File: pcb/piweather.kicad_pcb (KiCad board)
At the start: 4 copper layers, 65 x 64 mm, 22 parts, among them J1 Screw_Terminal_01x10, J10 Conn_01x03_Male, J11 Conn_01x03_Male, J12 Conn_01x02_Male, J2 Conn_01x08_Male, J3 Screw_Terminal_01x02, J4 Raspberry_Pi_2_3, J5 Conn_01x03_Male, J6 Conn_01x01_Male, J7 Conn_01x01_Male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

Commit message: started passive placement
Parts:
- added C10: GRM21BR60J476ME15K, Main:CAPC0805, F.Cu at (96.1, 78.3)
- added C11: CC0603KRX7R9BB104, Main:CAPC0603, F.Cu at (158.1, 82.4)
- added C12: GRM21BR60J476ME15K, Main:CAPC0805, F.Cu at (111.1, 56.0)
- added C13: CC0603KRX7R9BB104, Main:CAPC0603, F.Cu at (76.6, 108.8)
- added C3: CC0603KRX7R9BB333, Main:CAPC0603, F.Cu at (107.8, 107.3)
- added C4: CP, Capacitor_SMD:C_1206_3216Metric, F.Cu at (111.1, 53.3)
- added C5: CC0603KRX7R9BB104, Main:CAPC0603, F.Cu at (152.7, 85.6)
- added C6: CC0603KRX7R9BB104, Main:CAPC0603, F.Cu at (149.7, 87.7)
- added C7: CC0603KRX7R9BB104, Main:CAPC0603, F.Cu at (152.4, 87.7)
- added C8: CC0603KRX7R9BB104, Main:CAPC0603, F.Cu at (149.7, 89.3)
- added C9: CC0603KRX7R9BB104, Main:CAPC0603, F.Cu at (152.4, 89.3)
- added FB1: Ferrite_Bead_Small, Main:CAPC0603, F.Cu at (103.3, 101.0)
- added R1: RC0603FR-071K5L, Main:RESC0603, F.Cu at (166.6, 89.0)
- added R2: RC0603FR-0710KL, Main:RESC0603, F.Cu at (106.6, 106.0)
- added R3: RC0603FR-07475RL, Main:RESC0603, F.Cu at (162.6, 88.8)
- added R4: RC0603FR-0710KL, Main:RESC0603, F.Cu at (160.7, 84.1)
- added R5: RC0603FR-0710KL, Main:RESC0603, F.Cu at (162.3, 92.8)
- added R6: RC0603FR-071ML, Main:RESC0603, F.Cu at (106.1, 96.3)
- added Y1: Resonator, Main:RESONTATOR_450X200, F.Cu at (107.8, 98.3)
- moved U5 58.9 mm to (77.6, 111.8)
- moved U1 2.50 mm to (113.6, 102.8), turned to 45 degrees
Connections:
- J11 pad 1: (no net) -> GND
- J11 pad 2: (no net) -> /P0_TXD
- J11 pad 3: (no net) -> /P0_RXD
- J12 pad 1: (no net) -> /AC_L
- J12 pad 2: (no net) -> /AC_N
- J2 pad 1: (no net) -> /P1_3V3
- J2 pad 2: (no net) -> +5V
- J2 pad 6: (no net) -> /P1_RXD_HW_TXD
- J2 pad 7: (no net) -> /P1_TXD_HW_RXD
- J2 pad 8: (no net) -> GND
- J3 pad 1: (no net) -> /IN_24V
- J3 pad 2: (no net) -> GND
- J4 pad 1: (no net) -> +3V3
- J4 pad 10: (no net) -> /P0_RXD
- J4 pad 14: (no net) -> GND
- J4 pad 17: (no net) -> +3V3
- J4 pad 2: (no net) -> +5V
- J4 pad 20: (no net) -> GND
- J4 pad 25: (no net) -> GND
- J4 pad 3: (no net) -> /SDA
- J4 pad 30: (no net) -> GND
- J4 pad 34: (no net) -> GND
- J4 pad 39: (no net) -> GND
- J4 pad 4: (no net) -> +5V
- J4 pad 5: (no net) -> /SCL
- J4 pad 6: (no net) -> GND
- J4 pad 8: (no net) -> /P0_TXD
- J4 pad 9: (no net) -> GND
- J6 pad 1: (no net) -> +5V
- J7 pad 1: (no net) -> GND
- J8 pad 1: (no net) -> /USBD_P
- J9 pad 1: (no net) -> /USBD_N
- U1 pad 14: (no net) -> /P1_3V3
- U1 pad 18: (no net) -> GND
- U1 pad 2: (no net) -> /EEDATA
- U1 pad 23: (no net) -> /P1_RXD_HW_TXD
- U1 pad 24: (no net) -> /P1_TXD_HW_RXD
- U1 pad 25: (no net) -> GND
- U1 pad 3: (no net) -> /VCC_FTDI
- U1 pad 30: (no net) -> /P_DE
- U1 pad 31: (no net) -> +5V
- U1 pad 34: (no net) -> GND
- U1 pad 39: (no net) -> /P2_R
- U1 pad 4: (no net) -> +5V
- U1 pad 40: (no net) -> /P2_D
- U1 pad 41: (no net) -> /P2_~RE
- U1 pad 42: (no net) -> /VCC_FTDI
- U1 pad 43: (no net) -> /XTIN
- U1 pad 44: (no net) -> /XTOUT
- U1 pad 45: (no net) -> GND
- U1 pad 46: (no net) -> /AVCC
- U1 pad 47: (no net) -> GND
- U1 pad 5: (no net) -> /~RSTOUT
- U1 pad 6: (no net) -> /3V3OUT
- U1 pad 7: (no net) -> /USBD_P
- U1 pad 8: (no net) -> /USBD_N
- U1 pad 9: (no net) -> GND
- U2 pad 1: (no net) -> /AC_L
- U2 pad 14: (no net) -> GND
- U2 pad 16: (no net) -> +5V
- U2 pad 3: (no net) -> /AC_N
- U3 pad 1: (no net) -> /P2_R
- U3 pad 2: (no net) -> /P2_~RE
- U3 pad 3: (no net) -> /P_DE
- U3 pad 4: (no net) -> /P2_D
- U3 pad 5: (no net) -> GND
- U3 pad 8: (no net) -> +5V
- U4 pad 1: (no net) -> /IN_24V
- U4 pad 2: (no net) -> /IN_24V
- U4 pad 3: (no net) -> GND
- U4 pad 4: (no net) -> +5V
- U4 pad 5: (no net) -> +5V
- U4 pad 6: (no net) -> Net-(R4-Pad2)
- U4 pad 7: (no net) -> GND
- U5 pad 1: (no net) -> /SDA
- U5 pad 2: (no net) -> GND
- U5 pad 5: (no net) -> +3V3
- U5 pad 6: (no net) -> /SCL
- U5 pad 7: (no net) -> GND

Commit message: wip, more placement
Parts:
- added C1: GRM21BR60J476ME15K, Main:CAPC0805, F.Cu at (98.1, 52.5)
- added C2: GRM21BR60J476ME15K, Main:CAPC0805, F.Cu at (85.6, 53.3)
- added L1: L, Inductor_SMD:L_Wuerth_MAPI-3020, F.Cu at (90.1, 54.3)
- added R7: RC0603FR-071ML, Main:RESC0603, F.Cu at (97.1, 55.0)
- added R8: RC0603FR-0734KL, Main:RESC0603, F.Cu at (98.8, 55.0)
- added U6: TLV61046ADB, Package_TO_SOT_SMD:SOT-23-6, F.Cu at (94.1, 54.3)
- moved U3 26.8 mm to (121.8, 96.3)
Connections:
- net Net-(R4-Pad2) renamed /FB_DCDC

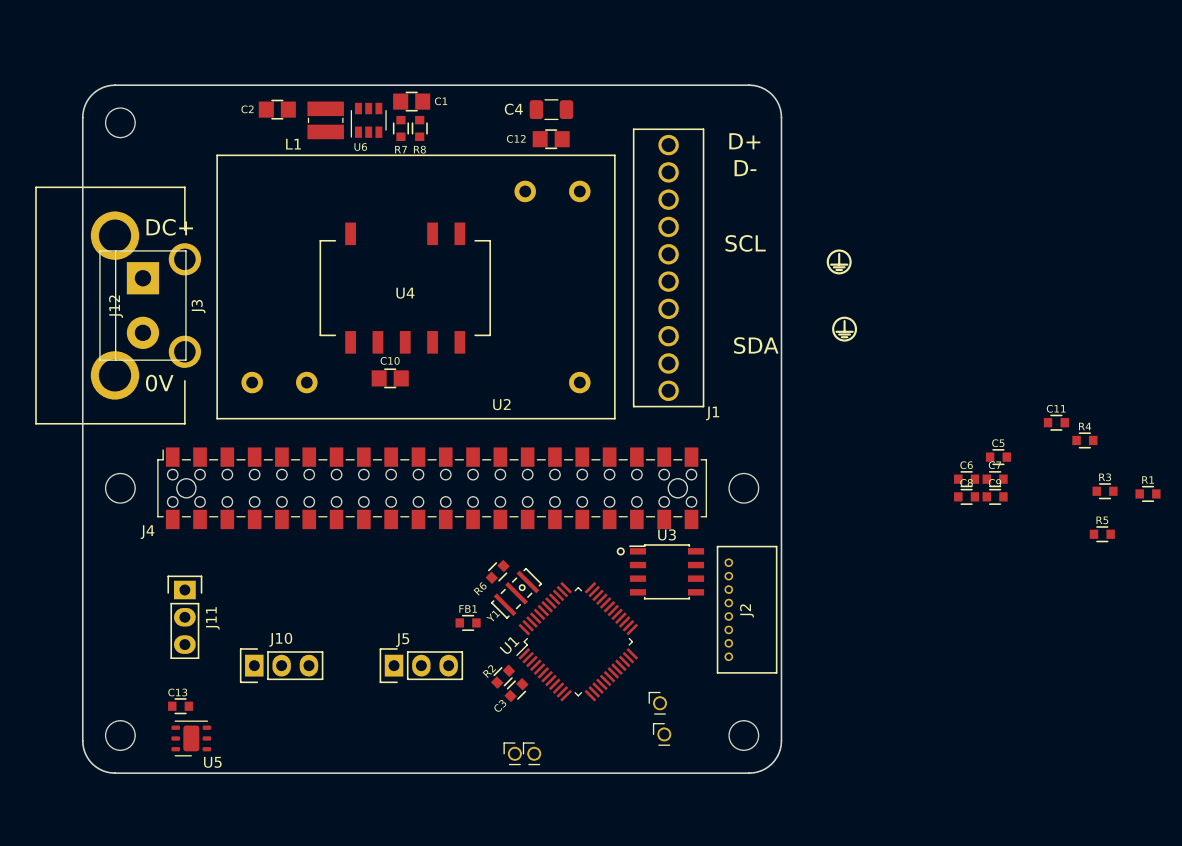
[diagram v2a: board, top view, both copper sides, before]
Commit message: updated placement, will start routing
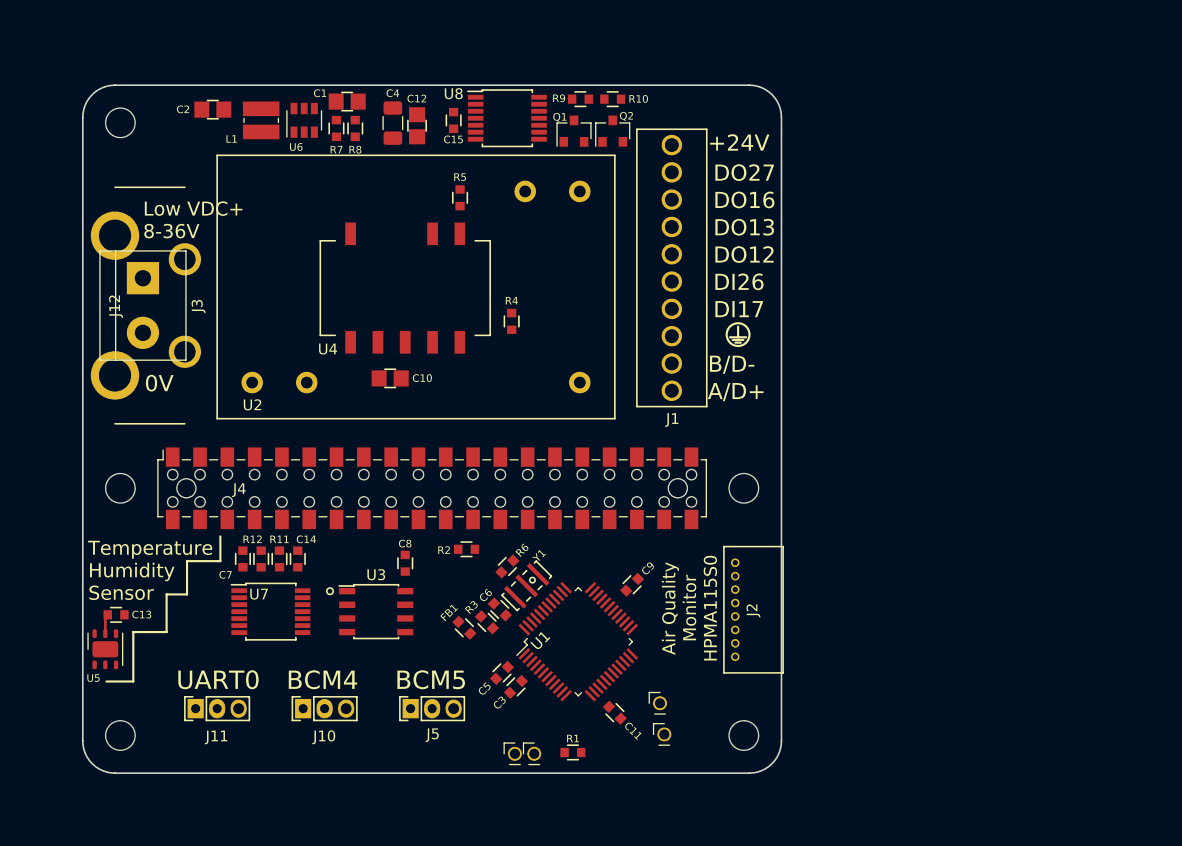
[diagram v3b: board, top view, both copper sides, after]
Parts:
- added A1: ART, pluggee:pluggeeLogo, B.Cu at (95.0, 66.7)
- added A2: ART, pluggee:pluggee-QRNEG-127X127, B.Cu at (82.8, 56.9)
- added A3: ART, Symbol:KiCad-Logo2_6mm_SilkScreen, B.Cu at (97.0, 56.9)
- added C14: CC0603KRX7R9BB104, Main:CAPC0603, F.Cu at (87.5, 95.1)
- added C15: CC0603KRX7R9BB104, Main:CAPC0603, F.Cu at (102.0, 54.3)
- added Q1: 2N7002, Package_TO_SOT_SMD:SOT-23, F.Cu at (113.2, 55.3)
- added Q2: 2N7002, Package_TO_SOT_SMD:SOT-23, F.Cu at (116.8, 55.3)
- added R10: RC0603FR-0730K1L, Main:RESC0603, F.Cu at (116.8, 52.3)
- added R11: RC0603FR-0730K1L, Main:RESC0603, F.Cu at (85.8, 95.1)
- added R12: RC0603FR-0730K1L, Main:RESC0603, F.Cu at (84.1, 95.1)
- added R9: RC0603FR-0730K1L, Main:RESC0603, F.Cu at (113.8, 52.3)
- added U7: 74HC14, Package_SO:TSSOP-14_4.4x5mm_P0.65mm, F.Cu at (85.0, 100.0)
- added U8: LM339, Package_SO:TSSOP-14_4.4x5mm_P0.65mm, F.Cu at (107.0, 54.1)
- J10, J11, J5: footprint Main:SOCKET254P-01X03-0705530002 -> Main:SOCKET200P-01X03-S3B-PH-K-S(LF)(SN)
- moved C7 70.4 mm to (82.4, 95.1), turned to 270 degrees
- moved R5 67.5 mm to (102.6, 61.5), turned to 90 degrees
- moved R3 58.8 mm to (105.1, 101.0), turned to 315 degrees
- moved R1 58.7 mm to (113.1, 113.1)
- moved R4 54.5 mm to (107.4, 73.0), turned to 90 degrees
- moved C8 52.6 mm to (97.5, 95.5), turned to 90 degrees
- moved C5 50.4 mm to (106.5, 105.7), turned to 225 degrees
- moved C11 49.1 mm to (117.0, 109.4), turned to 315 degrees
- moved C6 45.1 mm to (106.3, 99.8), turned to 135 degrees
- moved C9 34.8 mm to (118.6, 97.5), turned to 225 degrees
- moved U3 27.3 mm to (94.8, 100.0)
- moved C4 14.8 mm to (96.3, 54.5), turned to 90 degrees
- moved C12 12.5 mm to (98.6, 54.8), turned to 90 degrees
- moved R2 12.3 mm to (103.2, 94.2), turned to 180 degrees
- moved U5 11.5 mm to (69.6, 103.5), turned to 90 degrees
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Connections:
- C7 pad 1: +5V -> REF3V3
- J1 pad 1: (no net) -> RS485_A
- J1 pad 10: (no net) -> +24V
- J1 pad 2: (no net) -> RS485_B
- J1 pad 3: (no net) -> GND
- J1 pad 4: (no net) -> /DI17
- J1 pad 5: (no net) -> /DI26
- J1 pad 6: (no net) -> /DO12
- J1 pad 7: (no net) -> /DO13
- J1 pad 8: (no net) -> /DO16
- J1 pad 9: (no net) -> /DO27
- J10 pad 1: (no net) -> +3V3
- J10 pad 2: (no net) -> /BCM4_PIN7
- J10 pad 3: (no net) -> GND
- J4 pad 11: (no net) -> /BCM17_PIN11
- J4 pad 13: (no net) -> BCM27
- J4 pad 29: (no net) -> /BCM5_PIN29
- J4 pad 32: (no net) -> BCM12
- J4 pad 33: (no net) -> BCM13
- J4 pad 36: (no net) -> BCM16
- J4 pad 37: (no net) -> /BCM26_PIN37
- J4 pad 7: (no net) -> /BCM4_PIN7
- J5 pad 1: (no net) -> +3V3
- J5 pad 2: (no net) -> /BCM5_PIN29
- J5 pad 3: (no net) -> GND
- U3 pad 6: (no net) -> RS485_A
- U3 pad 7: (no net) -> RS485_B
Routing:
- net +3V3: track 0.00 -> 1.84 mm
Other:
- board text added: "+24V"
- board text added: "A/D+"
- board text added: "Air Quality Monitor HPMA115S0"
- board text added: "B/D-"
- board text added: "BCM4"
- board text added: "BCM5"
- board text added: "DI17"
- board text added: "DI26"
- board text added: "DO12"
- board text added: "DO13"
- board text added: "DO16"
- board text added: "DO27"
- board text added: "High Voltage Input : 85 - 264 VAC, 100 - 370 VDC Low Voltage Input : 8 - 36V"
- board text added: "Low VDC+ 8-36V"
- board text added: "PiWeather Zero v1.0 A complete RPi Zero/W base to monitor air with 24V control I/Os"
- board text added: "Temperature Humidity Sensor"
- board text added: "UART0"
- board text removed: "D+"
- board text removed: "D-"
- board text removed: "DC+"
- board text removed: "SCL"
- board text removed: "SDA"

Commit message: layout in progress
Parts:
- R6: value RC0603FR-071ML -> RC1206FR-071ML; footprint Main:RESC0603 -> Main:RESC1206
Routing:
- net +5V: track 0.00 -> 55.3 mm
- net /DO12: track 0.00 -> 37.6 mm, vias 0 -> 2
- net /IN_24V: track 0.00 -> 35.0 mm
- net +24V: track 0.00 -> 29.9 mm, vias 0 -> 1
- net /DO27: track 0.00 -> 29.5 mm, vias 0 -> 2
- net /DO13: track 0.00 -> 27.3 mm, vias 0 -> 1
- net /DO16: track 0.00 -> 26.2 mm, vias 0 -> 1
- net /DI17: track 0.00 -> 24.0 mm, vias 0 -> 1
- net /DI26: track 0.00 -> 18.1 mm, vias 0 -> 1
- net /AC_N: track 0.00 -> 17.6 mm
- net /USBD_P: track 0.00 -> 15.9 mm, vias 0 -> 1
- net /FB_DCDC: track 0.00 -> 13.7 mm
- net /USBD_N: track 0.00 -> 11.5 mm, vias 0 -> 1
- net /AC_L: track 0.00 -> 7.45 mm
- net /XTIN: track 0.00 -> 6.96 mm
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
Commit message: routing in progress
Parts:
- moved R2 10.5 mm to (105.3, 104.5), turned to 225 degrees
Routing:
- net +3V3: track 1.84 -> 100.8 mm, vias 0 -> 8
- net BCM13: track 0.00 -> 48.0 mm, vias 0 -> 4
- net BCM27: track 0.00 -> 47.9 mm, vias 0 -> 3
- net /BCM26_PIN37: track 0.00 -> 43.7 mm, vias 0 -> 3
- net BCM12: track 0.00 -> 39.5 mm, vias 0 -> 4
- net BCM16: track 0.00 -> 38.0 mm, vias 0 -> 3
- net /BCM5_PIN29: track 0.00 -> 29.3 mm, vias 0 -> 2
- net GND: track 0.00 -> 27.9 mm, vias 0 -> 18
- net /P0_RXD: track 0.00 -> 26.2 mm, vias 0 -> 1
- net /SDA: track 0.00 -> 25.8 mm, vias 0 -> 2
- net /P_DE: track 0.00 -> 25.5 mm, vias 0 -> 2
- net /P0_TXD: track 0.00 -> 25.4 mm, vias 0 -> 1
- net /P2_D: track 0.00 -> 24.0 mm, vias 0 -> 2
- net /BCM4_PIN7: track 0.00 -> 23.7 mm, vias 0 -> 2
- net /P2_R: track 0.00 -> 22.2 mm, vias 0 -> 2
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- added copper zone on B.Cu, net +3V3
- added copper zone on B.Cu, net +5V
- added copper zone on F.Cu, net GND

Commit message: preparing for first release
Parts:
- moved R1 5.69 mm to (109.5, 108.7), turned to 225 degrees
- moved C3 0.71 mm to (108.3, 107.5)
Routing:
- net ~BCM26: track 2.62 -> 77.3 mm, vias 0 -> 4
- net ~BCM17: track 2.05 -> 73.1 mm, vias 0 -> 3
- net REF3V3: track 12.1 -> 71.8 mm, vias 0 -> 3
- net RS485_B: track 0.00 -> 45.1 mm, vias 0 -> 2
- net RS485_A: track 0.00 -> 44.4 mm, vias 0 -> 2
- net /VCC_FTDI: track 4.81 -> 19.9 mm, vias 0 -> 4
- net /P1_3V3: track 1.95 -> 16.5 mm, vias 0 -> 1
- net /P1_RXD_HW_TXD: track 2.88 -> 16.4 mm, vias 0 -> 2
- net GND: track 27.9 -> 40.7 mm, vias 18 -> 24
- net /~RSTOUT: track 0.00 -> 8.17 mm, vias 0 -> 2
- net +5V: track 44.8 -> 47.3 mm, vias 11 -> 13
- net /P1_TXD_HW_RXD: track 14.6 -> 16.0 mm, vias 0 -> 2
- net /DI26: track 18.1 -> 19.5 mm
- net /3V3OUT: track 2.60 -> 2.02 mm
- added copper zone on In1.Cu, net GND
- added copper zone on In2.Cu, net GND
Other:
- rule pad_to_mask_clearance: 0.15 -> 0.1
- rule solder_mask_min_width: 0.25 -> 0.1
